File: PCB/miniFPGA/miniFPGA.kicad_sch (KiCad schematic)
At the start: 35 parts, among them J1 USB_B, J2 ICSP_FPGA, U2 MCP2221A-IP, U3 PIC16F13145-IP

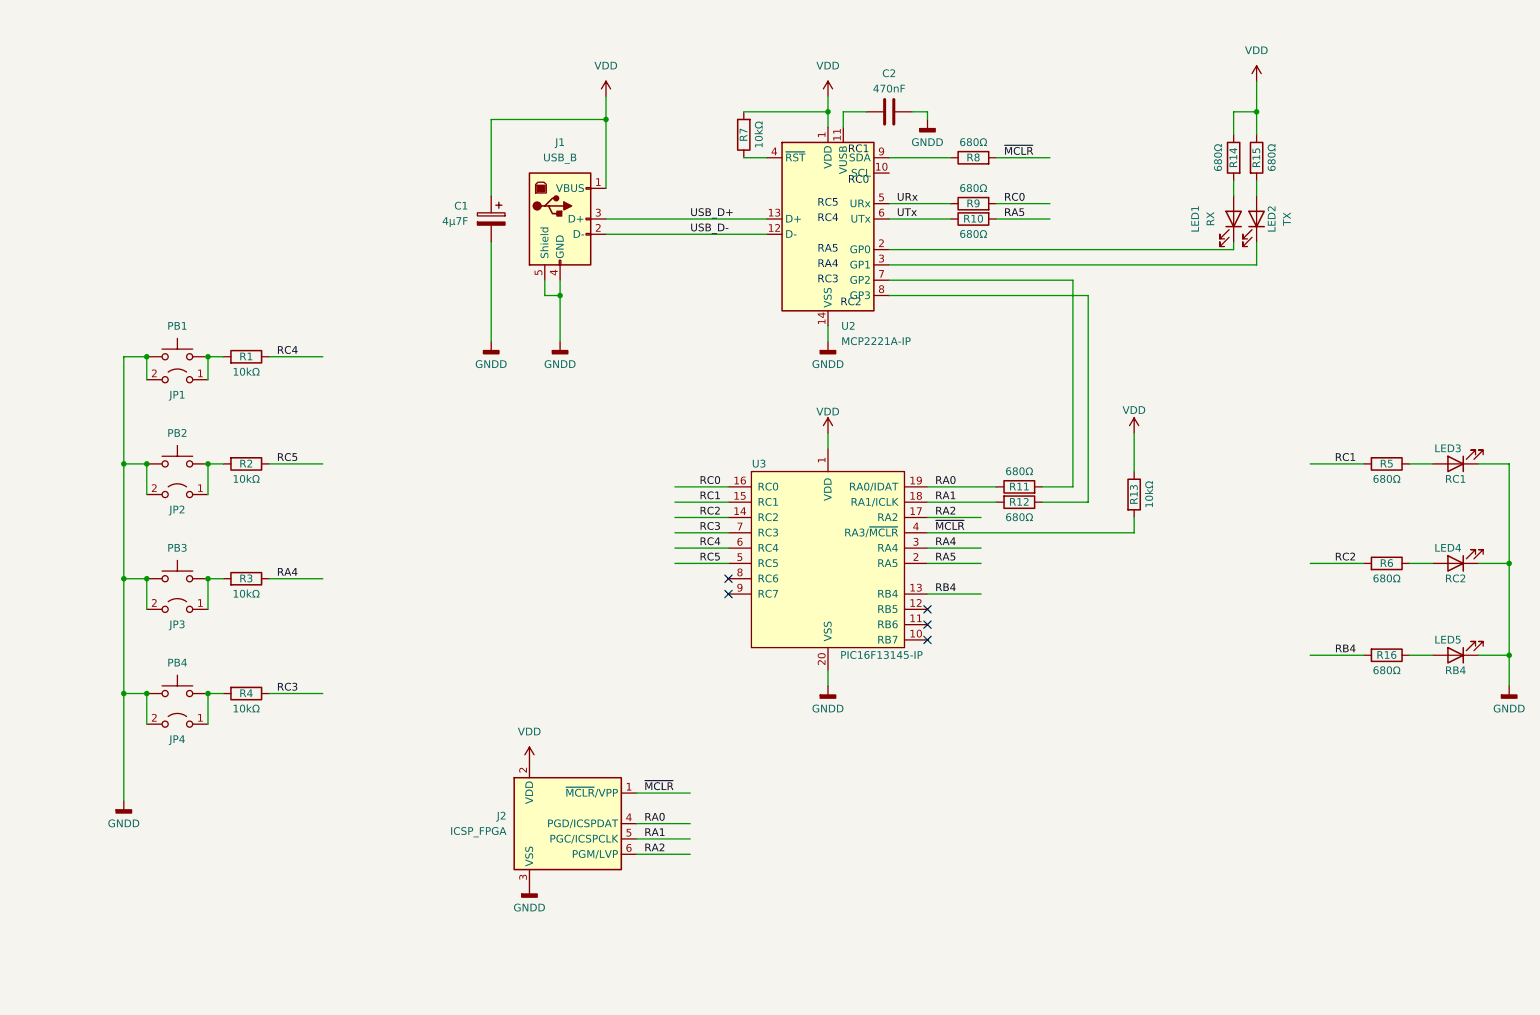
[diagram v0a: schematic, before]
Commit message: DCE / DTE clarification on RX/TX In schematics and PDF Fixes #41
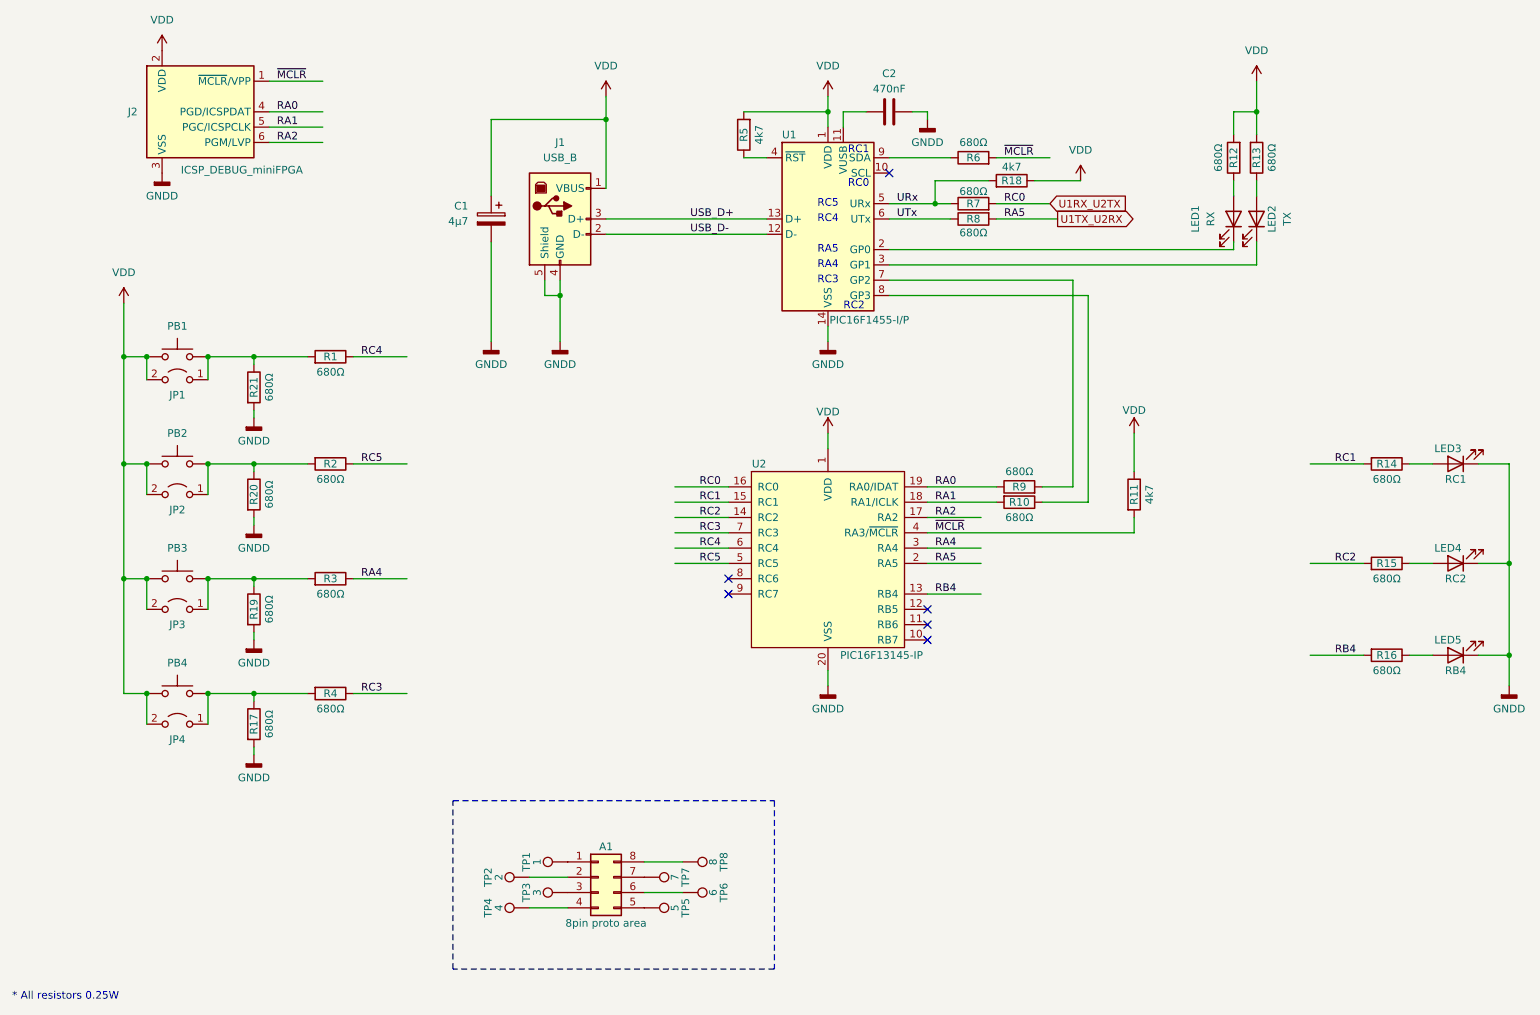
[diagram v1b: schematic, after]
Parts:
- added A1: 8pin proto area, Attila:8pin_proto, symbol Connector_Generic:Conn_02x04_Counter_Clockwise
- added R17, R19, R20, R21: 680Ω, Attila:R_Axial_L3.6mm_D1.6mm_P1.90mm_Vertical, symbol Device:R
- added R18: 4k7, Resistor_THT:R_Axial_DIN0204_L3.6mm_D1.6mm_P5.08mm_Horizontal, symbol Device:R
- added TP1: 1, TestPoint:TestPoint_Pad_1.5x1.5mm, symbol Connector:TestPoint
- added TP2: 2, TestPoint:TestPoint_Pad_D1.5mm, symbol Connector:TestPoint
- added TP3: 3, TestPoint:TestPoint_Pad_D1.5mm, symbol Connector:TestPoint
- added TP4: 4, TestPoint:TestPoint_Pad_D1.5mm, symbol Connector:TestPoint
- added TP5: 5, TestPoint:TestPoint_Pad_D1.5mm, symbol Connector:TestPoint
- added TP6: 6, TestPoint:TestPoint_Pad_D1.5mm, symbol Connector:TestPoint
- added TP7: 7, TestPoint:TestPoint_Pad_D1.5mm, symbol Connector:TestPoint
- added TP8: 8, TestPoint:TestPoint_Pad_D1.5mm, symbol Connector:TestPoint
- C1: value 4µ7F -> 4µ7
- J2: value ICSP_FPGA -> ICSP_DEBUG_miniFPGA
- PB1, PB2, PB3, PB4: Farnell (none) -> https://at.farnell.com/alcoswitch-te-connectivity/1825910-1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
- R1, R2, R3, R4: value 10kΩ -> 680Ω; footprint Resistor_THT:R_Axial_DIN0204_L3.6mm_D1.6mm_P5.08mm_Horizontal -> Attila:R_Axial_L3.6mm_D1.6mm_P1.90mm_Vertical
- R11: renamed from R13; value 10kΩ -> 4k7
- R5: renamed from R7; value 10kΩ -> 4k7
- U1: renamed from U2; value MCP2221A-IP -> PIC16F1455-I/P
- renumbered R12 to R10, R14 to R12, R15 to R13, R5 to R14, R6 to R15, R8 to R6, R9 to R7, R10 to R8, R11 to R9, U3 to U2
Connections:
- net GNDD: now also R17.2, R19.2, R20.2, R21.2; no longer JP1.2 (B), JP2.2 (B), JP3.2 (B), JP4.2 (B), PB1.2, PB2.2, PB3.2, PB4.2
- net URx: now also R18.2
- net VDD: now also JP1.2 (B), JP2.2 (B), JP3.2 (B), JP4.2 (B), PB1.2, PB2.2, PB3.2, PB4.2, R12.2, R13.2, R18.1; no longer R12.1, R13.1
- net at LED1.2 (A): now also R12.1; no longer R12.2
- net at JP1.1 (A), PB1.1, R1.2: now also R21.1
- net at JP3.1 (A), PB3.1, R3.2: now also R19.1
- net at JP2.1 (A), PB2.1, R2.2: now also R20.1
- net at JP4.1 (A), PB4.1, R4.2: now also R17.1
- net at LED2.2 (A): now also R13.1; no longer R13.2
- net RA5 renamed U1TX_U2RX
- net RC0 renamed U1RX_U2TX
- new net: A1.5 (Pin_5), TP5.1
- new net: A1.7 (Pin_7), TP7.1
- new net: A1.1 (Pin_1), TP1.1
- new net: A1.2 (Pin_2), TP2.1
- new net: A1.3 (Pin_3), TP3.1
- new net: A1.4 (Pin_4), TP4.1
- new net: A1.6 (Pin_6), TP6.1
- new net: A1.8 (Pin_8), TP8.1
- no-connect marks 5 -> 6
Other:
- note added: "* All resistors 0.25W"
- moved on the sheet: J2, R1, R12, R2, R3, R4
